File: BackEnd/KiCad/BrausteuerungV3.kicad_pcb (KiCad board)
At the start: 2 copper layers, 55 x 60 mm, 13 parts, among them IC1 DS18B20, J1 KHTaster, J2 myPiezzo, J3 Transmitter433MHz, J4 HC-06, P1 CONN_01X02, U1 arduino_nano

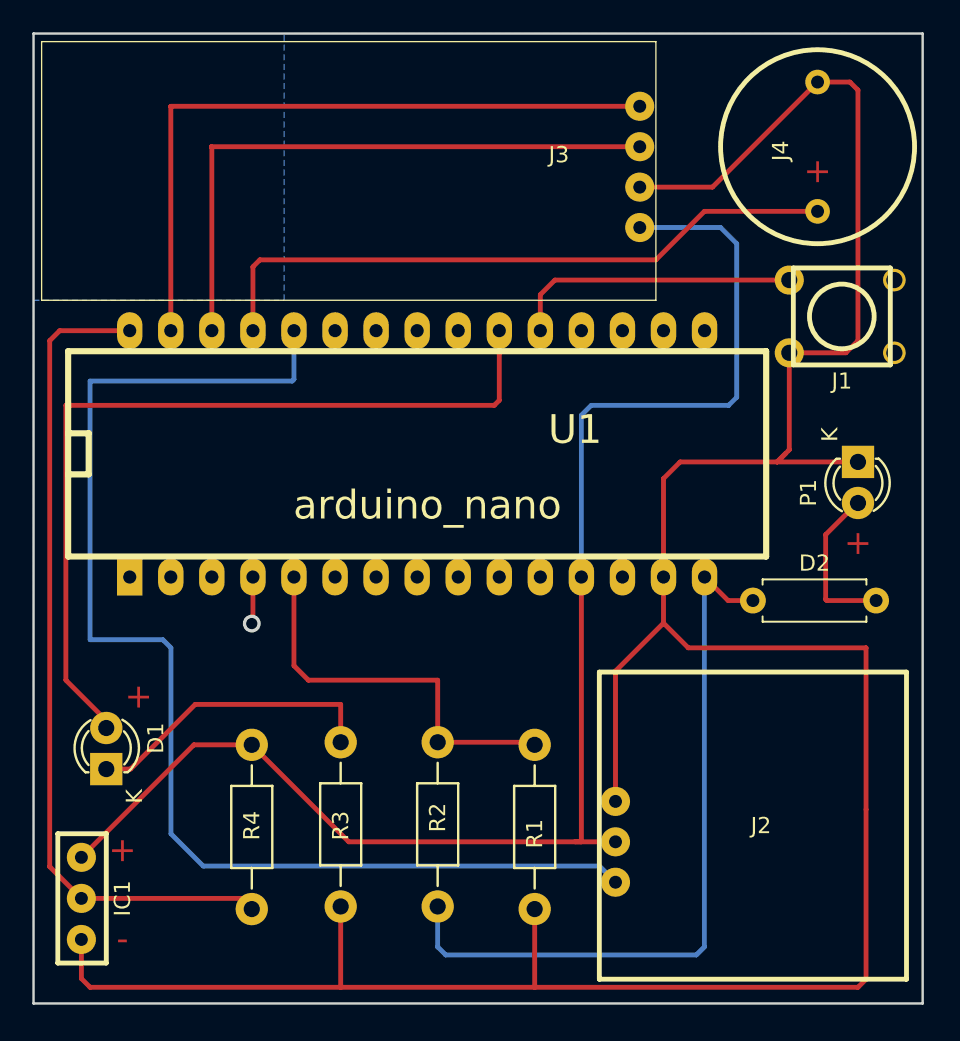
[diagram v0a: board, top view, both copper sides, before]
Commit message: some HC-06 need a circuit leveler
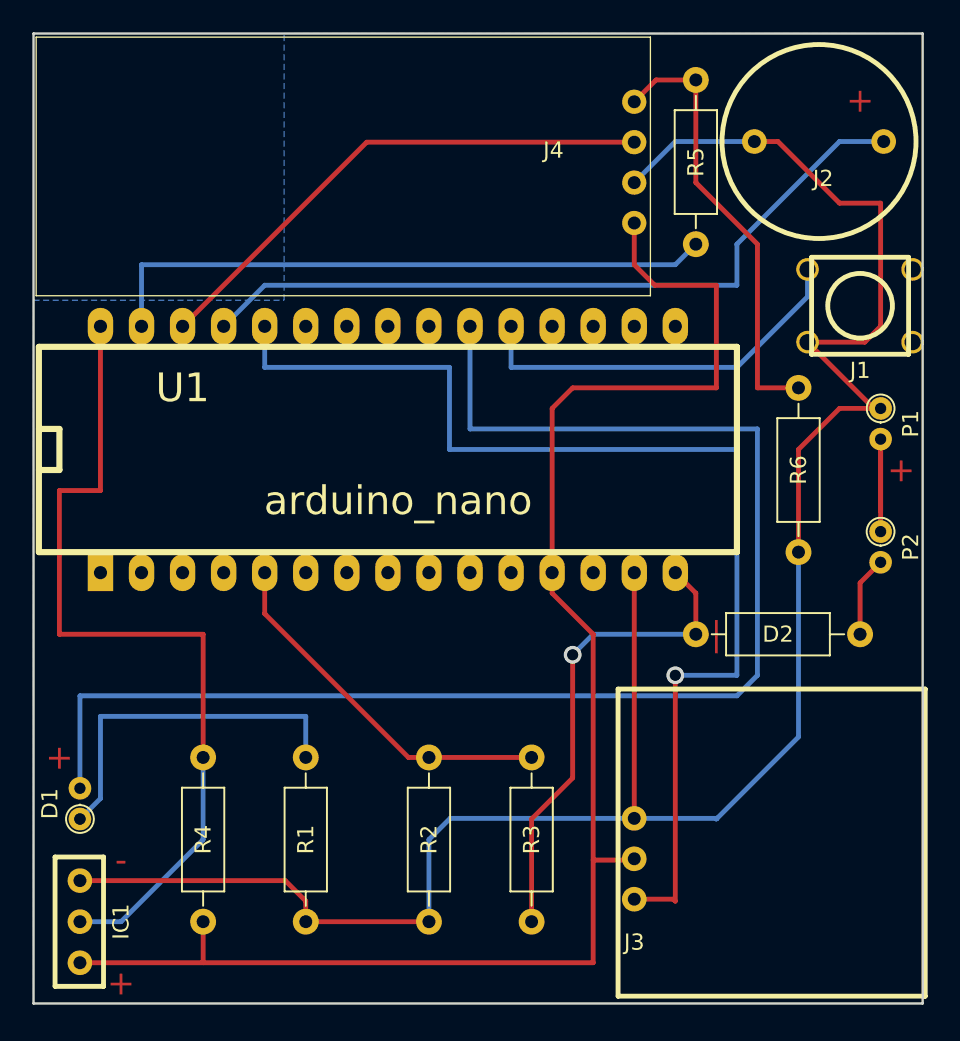
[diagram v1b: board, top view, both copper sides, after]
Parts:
- added P2: Switch, Resistors_THT:R_Axial_DIN0204_L3.6mm_D1.6mm_P1.90mm_Vertical, F.Cu at (152.4, 130.8)
- added R5: 1K, Resistors_THT:R_Axial_DIN0207_L6.3mm_D2.5mm_P10.16mm_Horizontal, F.Cu at (141.0, 102.9)
- added R6: 2K, Resistors_THT:R_Axial_DIN0207_L6.3mm_D2.5mm_P10.16mm_Horizontal, F.Cu at (147.3, 121.9)
- D1: footprint LEDs:LED-3MM -> Resistors_THT:R_Axial_DIN0204_L3.6mm_D1.6mm_P1.90mm_Vertical
- D2: footprint Resistors_ThroughHole:R_Axial_DIN0207_L6.3mm_D2.5mm_P7.62mm_Horizontal -> Resistors_THT:R_Axial_DIN0207_L6.3mm_D2.5mm_P10.16mm_Horizontal
- J2: footprint Transmitter433MHz:Transmitter433MHz -> myPiezzo:PIEZZO
- J3: footprint HC-06:HC-06 -> Transmitter433MHz:Transmitter433MHz
- J4: footprint myPiezzo:PIEZZO -> HC-06:HC-06
- P1: value CONN_01X02 -> Power 9V; footprint LEDs:LED-3MM -> Resistors_THT:R_Axial_DIN0204_L3.6mm_D1.6mm_P1.90mm_Vertical
- R1, R2, R3, R4: footprint Resistors_ThroughHole:Resistor_Horizontal_RM10mm -> Resistors_THT:R_Axial_DIN0207_L6.3mm_D2.5mm_P10.16mm_Horizontal
- moved J2 40.3 mm to (148.6, 106.7)
- moved J3 36.6 mm to (137.2, 146.1), turned to 0 degrees
- moved R1 17.9 mm to (116.8, 154.9), turned to 90 degrees
- moved R3 11.8 mm to (130.8, 154.9)
- moved J4 11.6 mm to (137.2, 109.2), turned to 180 degrees
- moved R4 11.3 mm to (110.5, 154.9), turned to 90 degrees
- moved R2 9.24 mm to (124.5, 144.8), turned to 270 degrees
- moved IC1 5.37 mm to (100.3, 154.9), turned to 90 degrees
- moved D2 4.10 mm to (141.0, 137.2)
- moved P1 3.59 mm to (152.4, 123.2)
- moved D1 3.49 mm to (102.9, 148.6)
- moved U1 1.83 mm to (123.2, 125.7)
- moved J1 1.31 mm to (151.1, 116.8)
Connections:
- D2 pad 2: +9V -> Net-(D2-Pad2)
- J2 pad 2: (no net) -> GNDREF
- J3 pad 2: GNDREF -> Net-(IC1-Pad3)
- J3 pad 3: (no net) -> GNDREF
- R1 pad 1: (no net) -> GNDREF
- R1 pad 2: GNDREF -> Net-(D1-Pad1)
- R2 pad 2: (no net) -> GNDREF
- R3 pad 1: GNDREF -> Net-(D2-Pad1)
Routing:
- net Net-(J3-Pad1): track 8.17 -> 71.2 mm, vias 0 -> 1
- net GNDREF: track 179.8 -> 129.8 mm, vias 0 -> 2
- net Net-(D1-Pad2): track 52.2 -> 87.5 mm, vias 0 -> 1
- net Net-(J2-Pad1): track 77.9 -> 47.1 mm
- net Net-(J4-Pad4): track 0.00 -> 27.5 mm, vias 0 -> 1
- net Net-(D2-Pad1): track 48.4 -> 30.0 mm
- net Net-(IC1-Pad3): track 105.6 -> 97.4 mm
- net Net-(R2-Pad1): track 29.5 -> 22.7 mm, vias 1 -> 0
- net Net-(J1-Pad1): track 18.0 -> 24.4 mm, vias 0 -> 1
- net Net-(J4-Pad3): track 37.9 -> 32.7 mm
- net Net-(D2-Pad2): track 0.00 -> 4.98 mm
- net Net-(R5-Pad2): track 42.9 -> 38.6 mm, vias 0 -> 1
- net Net-(U1-Pad4): track 2.91 -> 0.00 mm, vias 1 -> 0
- net Net-(IC1-Pad2): track 51.3 -> 52.9 mm, vias 0 -> 1
- net Net-(D1-Pad1): track 21.0 -> 22.1 mm, vias 0 -> 1
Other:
- board text added: "|"

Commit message: reverted to circuit without spannungsteiler HC06
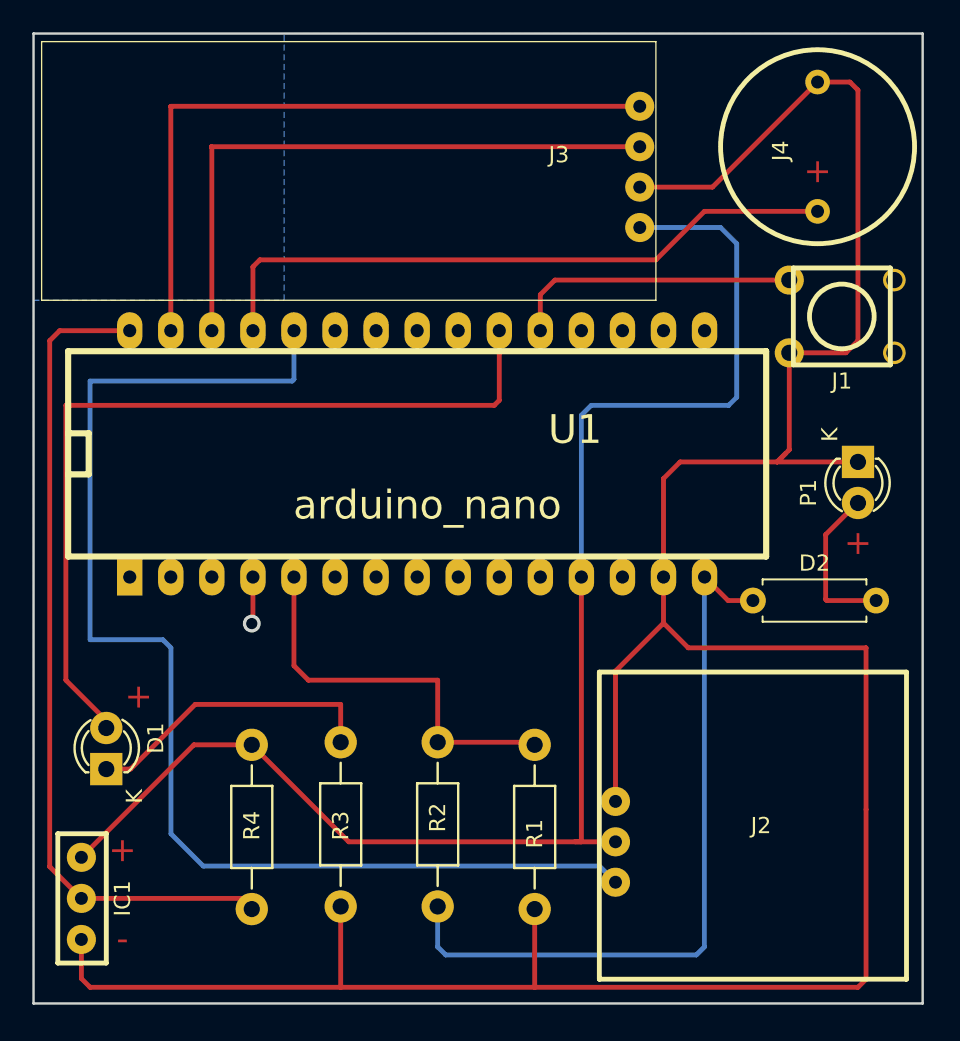
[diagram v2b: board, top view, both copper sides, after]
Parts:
- removed P2: Switch, Resistors_THT:R_Axial_DIN0204_L3.6mm_D1.6mm_P1.90mm_Vertical
- removed R5: 1K, Resistors_THT:R_Axial_DIN0207_L6.3mm_D2.5mm_P10.16mm_Horizontal
- removed R6: 2K, Resistors_THT:R_Axial_DIN0207_L6.3mm_D2.5mm_P10.16mm_Horizontal
- D1: footprint Resistors_THT:R_Axial_DIN0204_L3.6mm_D1.6mm_P1.90mm_Vertical -> LEDs:LED-3MM
- D2: footprint Resistors_THT:R_Axial_DIN0207_L6.3mm_D2.5mm_P10.16mm_Horizontal -> Resistors_ThroughHole:R_Axial_DIN0207_L6.3mm_D2.5mm_P7.62mm_Horizontal
- J2: footprint myPiezzo:PIEZZO -> Transmitter433MHz:Transmitter433MHz
- J3: footprint Transmitter433MHz:Transmitter433MHz -> HC-06:HC-06
- J4: footprint HC-06:HC-06 -> myPiezzo:PIEZZO
- P1: value Power 9V -> CONN_01X02; footprint Resistors_THT:R_Axial_DIN0204_L3.6mm_D1.6mm_P1.90mm_Vertical -> LEDs:LED-3MM
- R1, R2, R3, R4: footprint Resistors_THT:R_Axial_DIN0207_L6.3mm_D2.5mm_P10.16mm_Horizontal -> Resistors_ThroughHole:Resistor_Horizontal_RM10mm
- moved J2 40.3 mm to (136.0, 145.0)
- moved J3 36.6 mm to (137.5, 109.5), turned to 180 degrees
- moved R1 17.9 mm to (131.0, 144.0), turned to 270 degrees
- moved R3 11.8 mm to (119.0, 154.0)
- moved J4 11.6 mm to (148.5, 107.0), turned to 270 degrees
- moved R4 11.3 mm to (113.5, 144.0), turned to 270 degrees
- moved R2 9.24 mm to (125.0, 154.0), turned to 90 degrees
- moved IC1 5.37 mm to (105.5, 153.5), turned to 270 degrees
- moved D2 4.10 mm to (144.5, 135.1)
- moved P1 3.59 mm to (151.0, 126.5)
- moved D1 3.49 mm to (104.5, 145.5)
- moved U1 1.83 mm to (125.0, 126.0)
- moved J1 1.31 mm to (150.0, 117.5)
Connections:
- D2 pad 2: Net-(D2-Pad2) -> +9V
- J2 pad 2: GNDREF -> (no net)
- J3 pad 2: Net-(IC1-Pad3) -> GNDREF
- J3 pad 3: GNDREF -> (no net)
- R1 pad 1: GNDREF -> (no net)
- R1 pad 2: Net-(D1-Pad1) -> GNDREF
- R2 pad 2: GNDREF -> (no net)
- R3 pad 1: Net-(D2-Pad1) -> GNDREF
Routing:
- net Net-(J3-Pad1): track 71.2 -> 8.17 mm, vias 1 -> 0
- net GNDREF: track 129.8 -> 179.8 mm, vias 2 -> 0
- net Net-(D1-Pad2): track 87.5 -> 52.2 mm, vias 1 -> 0
- net Net-(J2-Pad1): track 47.1 -> 77.9 mm
- net Net-(J4-Pad4) (its old number): track 27.5 -> 0.00 mm, vias 1 -> 0
- net Net-(D2-Pad1): track 30.0 -> 48.4 mm
- net Net-(IC1-Pad3): track 97.4 -> 105.6 mm
- net Net-(R2-Pad1): track 22.7 -> 29.5 mm, vias 0 -> 1
- net Net-(J1-Pad1): track 24.4 -> 18.0 mm, vias 1 -> 0
- net Net-(J4-Pad3): track 32.7 -> 37.9 mm
- net Net-(D2-Pad2): track 4.98 -> 0.00 mm
- net Net-(J4-Pad4): track 38.6 -> 42.9 mm, vias 1 -> 0
- net Net-(U1-Pad4): track 0.00 -> 2.91 mm, vias 0 -> 1
- net Net-(IC1-Pad2): track 52.9 -> 51.3 mm, vias 1 -> 0
- net Net-(D1-Pad1): track 22.1 -> 21.0 mm, vias 1 -> 0
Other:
- board text removed: "|"
